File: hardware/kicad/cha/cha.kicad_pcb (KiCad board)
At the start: 4 copper layers, 173 x 134 mm, 115 parts, among them J1 AES_CHA, J2 CONF C, J3 CONF SM, J4 Câble PROG-CHA, U1 AMS1117-3.3, U10 74AHCT1G32, U11 74LVC1G07, U12 iCE40HX4K-TQ144, U13 AS4C32M16SB-6TIN, U14 iCE40HX4K-TQ144, U15 IS61WV10248EDBLL-10TLI, U2 AP2112K-1.2, U3 74LVC16244A, U4 74LVC16244A, U5 74LVC16244A, U6 74LVC16244A, U7 74AHCT16244, U8 74AHCT16244, U9 74AHCT244, X1 25 MHz 3,3 V, X2 25 MHz 3,3 V

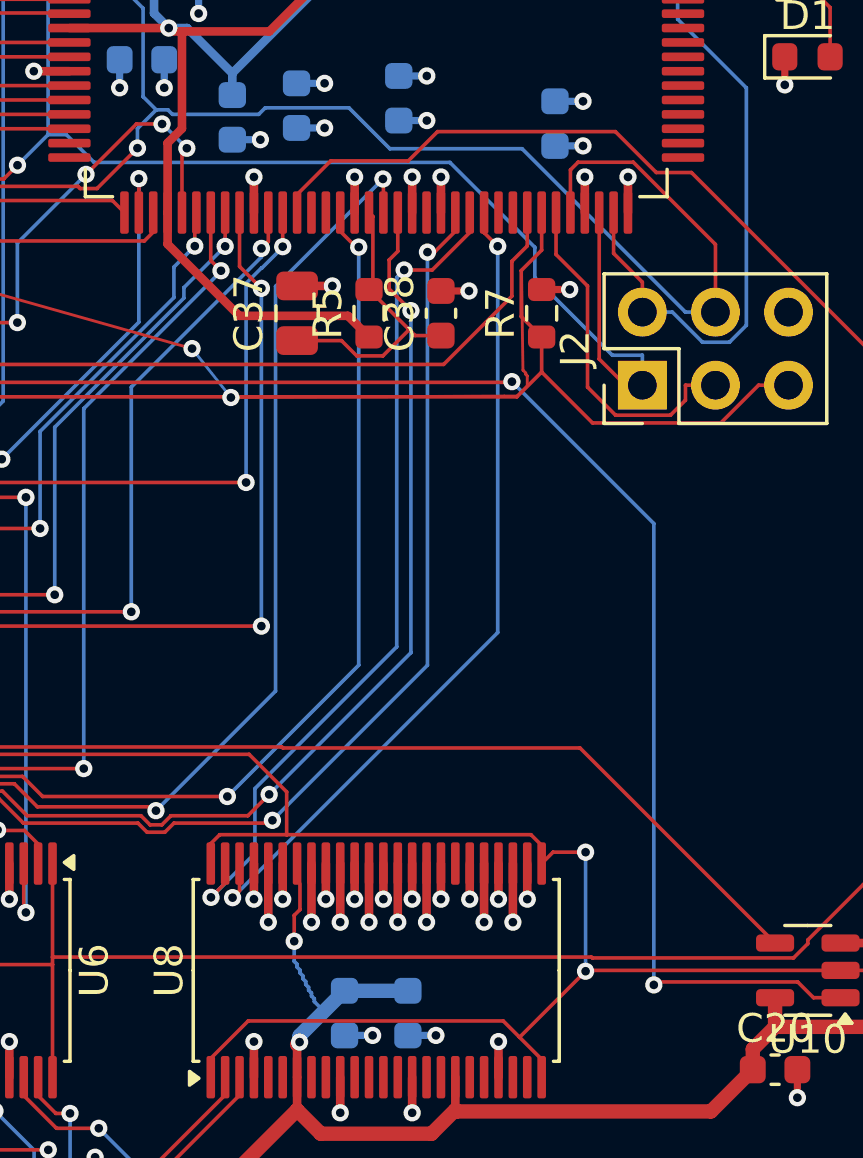
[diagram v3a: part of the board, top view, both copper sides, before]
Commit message: Carte CHA entièrement routée (dernière liaison : +5V de U8)
Sous U8 (2 canaux utilisés sur 16), les vias de masse des entrées
inutilisées enfermaient la broche 31 (+5V). La broche 32 (masse) est
reliée à sa voisine 33 au lieu d'avoir son propre via, ce qui libère
le passage ; +5V routé par le routeur de finition. DRC des deux cartes :
aucune liaison manquante, aucune violation de cuivre.

Co-Authored-By: Claude Opus 5.5 <noreply@anthropic.com>
Claude-Session: https://claude.ai/code/session_01WKfXP1YJ8otGxZ5dsY6Agh
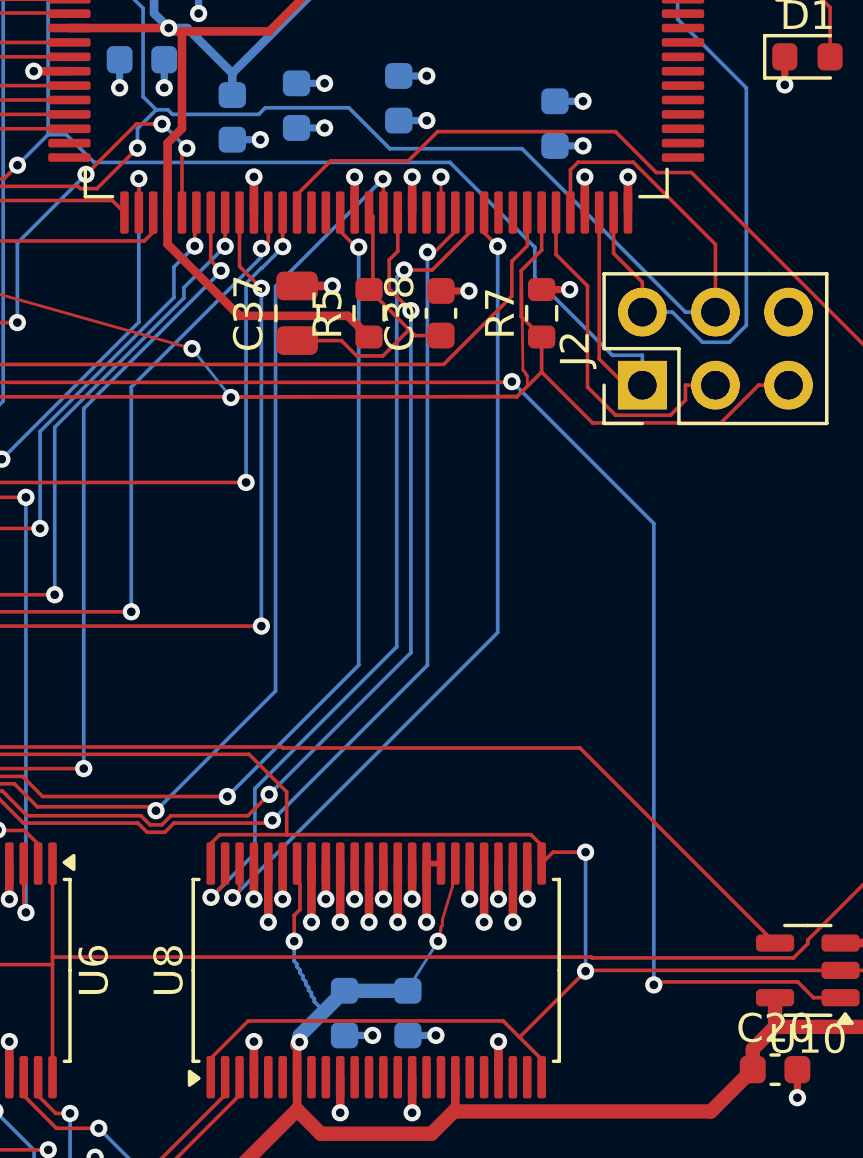
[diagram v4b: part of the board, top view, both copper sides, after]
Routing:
- net +5V: track 249.0 -> 252.9 mm, vias 10 -> 11
- net GND: track 280.6 -> 278.8 mm, vias 196 -> 195
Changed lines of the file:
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@@
   (segment (start 147.3861 152.3) (end 154.6675 145.0186) (width 0.5) (layer "F.Cu") (net 3))
   (segment (start 114.4486 129.1682) (end 98.7693 129.1682) (width 0.5) (layer "F.Cu") (net 3))
+  (segment (start 194.3 133.2375) (end 194.65 132.0875) (width 0.1) (layer "F.Cu") (net 3))
   (segment (start 147.3685 158.4735) (end 144.8815 158.4735) (width 0.5) (layer "F.Cu") (net 3))
   (segment (start 115.0342 129.7538) (end 115.9427 128.8453) (width 0.5) (layer "F.Cu") (net 3))
@@
   (segment (start 144.3732 152.3) (end 137.8767 145.8035) (width 0.5) (layer "F.Cu") (net 3))
   (segment (start 121.25 137.4558) (end 121.25 137.2725) (width 0.5) (layer "F.Cu") (net 3))
+  (segment (start 194.3 133.4375) (end 194.3 133.2375) (width 0.1) (layer "F.Cu") (net 3))
   (segment (start 115.9427 128.8453) (end 119.9477 128.8453) (width 0.5) (layer "F.Cu") (net 3))
   (segment (start 126.75 130.1476) (end 126.75 131.2875) (width 0.3004) (layer "F.Cu") (net 3))
+  (segment (start 194.15 133.9875) (end 194.25 133.5875) (width 0.1) (layer "F.Cu") (net 3))
   (segment (start 121.25 137.5726) (end 121.25 138.7125) (width 0.3004) (layer "F.Cu") (net 3))
   (segment (start 190.0739 140.6763) (end 189.25 139.8524) (width 0.5) (layer "F.Cu") (net 3))
+  (segment (start 194.65 132.0875) (end 194.65 131.9875) (width 0.1) (layer "F.Cu") (net 3))
   (segment (start 126.6515 130.0491) (end 125.9519 130.0491) (width 0.5) (layer "F.Cu") (net 3))
   (segment (start 115.0342 129.7538) (end 114.4486 129.1682) (width 0.5) (layer "F.Cu") (net 3))
@@
   (segment (start 126.75 139.8524) (end 126.75 138.7125) (width 0.3004) (layer "F.Cu") (net 3))
   (segment (start 147.795 158.9) (end 147.3685 158.4735) (width 0.5) (layer "F.Cu") (net 3))
+  (segment (start 194.25 133.5875) (end 194.25 133.4875) (width 0.1) (layer "F.Cu") (net 3))
   (segment (start 95.8133 132.1242) (end 95.8625 132.075) (width 0.4006) (layer "F.Cu") (net 3))
   (segment (start 189.25 137.5796) (end 189.25 138.7125) (width 0.3004) (layer "F.Cu") (net 3))
@@
   (segment (start 121.25 130.1476) (end 121.25 131.2875) (width 0.3004) (layer "F.Cu") (net 3))
   (segment (start 205.8625 136.9625) (end 205.0875 137.7375) (width 0.5) (layer "F.Cu") (net 3))
+  (segment (start 194.25 133.4875) (end 194.3 133.4375) (width 0.1) (layer "F.Cu") (net 3))
   (via (at 144.1433 160.3551) (size 0.6) (drill 0.3) (layers "F.Cu" "B.Cu") (net 3))
+  (via (at 194.15 133.9875) (size 0.6) (drill 0.3) (layers "F.Cu" "B.Cu") (net 3))
   (via (at 132.4705 145.8035) (size 0.6) (drill 0.3) (layers "F.Cu" "B.Cu") (net 3))
   (via (at 189.3373 137.4923) (size 0.6) (drill 0.3) (layers "F.Cu" "B.Cu") (net 3))
@@
   (segment (start 189.35 134.9875) (end 189.35 135.0875) (width 0.127) (layer "B.Cu") (net 3))
   (segment (start 193.1 135.71) (end 190.9 135.71) (width 0.5) (layer "B.Cu") (net 3))
+  (segment (start 193.2 135.4875) (end 194.15 133.9875) (width 0.1) (layer "B.Cu") (net 3))
   (segment (start 144.1433 160.3551) (end 144.3732 160.1252) (width 0.5) (layer "B.Cu") (net 3))
   (segment (start 189.75 135.8875) (end 189.85 135.9875) (width 0.127) (layer "B.Cu") (net 3))
@@
   (segment (start 101.338 91.25) (end 101.3375 91.25) (width 0.127) (layer "F.Cu") (net 162))
   (segment locked (start 162.25 131.2875) (end 162.25 132.525) (width 0.3) (layer "F.Cu") (net 162))
-  (segment (start 194.25 108.662) (end 194.25 108.6625) (width 0.127) (layer "F.Cu") (net 162))
   (segment locked (start 188.25 131.2875) (end 188.25 133.324999) (width 0.3) (layer "F.Cu") (net 162))
   (segment locked (start 189.75 82.8875) (end 190.975 82.8875) (width 0.3) (layer "F.Cu") (net 162))
@@
   (segment locked (start 190.75 131.2875) (end 190.75 133.324999) (width 0.3) (layer "F.Cu") (net 162))
   (segment locked (start 197.25 131.2875) (end 197.25 132.525) (width 0.3) (layer "F.Cu") (net 162))
-  (segment (start 194.25 131.288) (end 194.25 131.2875) (width 0.127) (layer "F.Cu") (net 162))
   (segment (start 189.75 131.288) (end 189.75 131.2875) (width 0.127) (layer "F.Cu") (net 162))
   (segment locked (start 193.25 131.2875) (end 193.25 132.525) (width 0.3) (layer "F.Cu") (net 162))
@@
   (segment locked (start 114.25 108.6625) (end 114.25 107.425) (width 0.3) (layer "F.Cu") (net 162))
   (segment locked (start 172.75 138.7125) (end 172.75 137.475) (width 0.3) (layer "F.Cu") (net 162))
-  (segment locked (start 194.25 131.2875) (end 194.25 132.525) (width 0.3) (layer "F.Cu") (net 162))
   (segment (start 175.25 138.712) (end 175.25 138.7125) (width 0.127) (layer "F.Cu") (net 162))
   (segment (start 171.25 138.712) (end 171.25 138.7125) (width 0.127) (layer "F.Cu") (net 162))
@@
   (segment locked (start 114.75 83.0625) (end 115.725 83.0625) (width 0.25) (layer "F.Cu") (net 162))
   (segment locked (start 173.75 138.7125) (end 173.75 137.475) (width 0.3) (layer "F.Cu") (net 162))
-  (segment locked (start 194.25 108.6625) (end 194.25 107.425) (width 0.3) (layer "F.Cu") (net 162))
   (segment locked (start 101.3375 91.25) (end 102.575 91.25) (width 0.3) (layer "F.Cu") (net 162))
+  (segment locked (start 194.25 131.2875) (end 193.75 131.2875) (width 0.2) (layer "F.Cu") (net 162))
   (segment (start 208.538 97.85) (end 208.5375 97.85) (width 0.127) (layer "F.Cu") (net 162))
   (segment locked (start 191.25 131.2875) (end 191.25 132.525) (width 0.3) (layer "F.Cu") (net 162))
@@
   (segment locked (start 111.25 108.6625) (end 111.25 107.425) (width 0.3) (layer "F.Cu") (net 162))
   (segment locked (start 159.25 131.2875) (end 159.25 130.049999) (width 0.3) (layer "F.Cu") (net 162))
+  (segment (start 194.25 107.725) (end 194.25 107.925) (width 0.1) (layer "F.Cu") (net 162))
   (segment locked (start 187.75 131.2875) (end 187.75 132.525) (width 0.3) (layer "F.Cu") (net 162))
   (segment locked (start 145.505 159.4) (end 145.505 160.375) (width 0.25) (layer "F.Cu") (net 162))
@@
   (via locked (at 199.447358 98.505665) (size 0.6) (drill 0.3) (layers "F.Cu" "B.Cu") (net 162))
   (via locked (at 170.75 137.475) (size 0.6) (drill 0.3) (layers "F.Cu" "B.Cu") (net 162))
-  (via locked (at 194.25 132.525) (size 0.6) (drill 0.3) (layers "F.Cu" "B.Cu") (net 162))
   (via locked (at 143.825 147.4) (size 0.6) (drill 0.3) (layers "F.Cu" "B.Cu") (net 162))
   (via locked (at 178.25 137.475) (size 0.6) (drill 0.3) (layers "F.Cu" "B.Cu") (net 162))

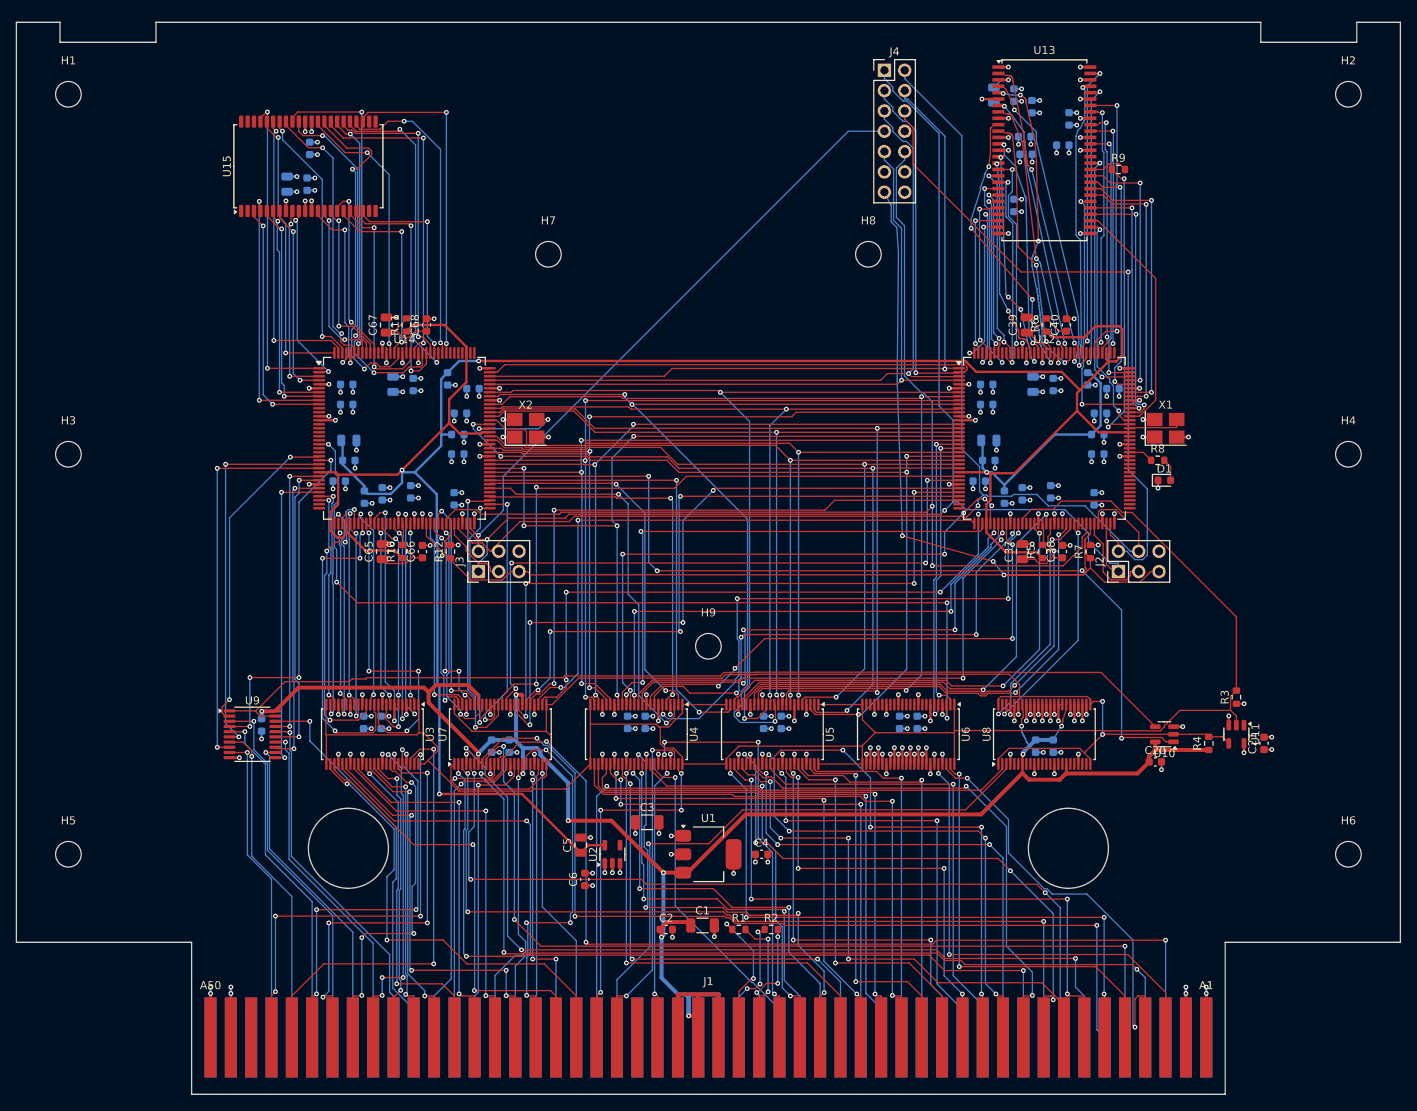
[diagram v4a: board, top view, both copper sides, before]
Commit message: Régulateur 3,3 V à découpage, horloge SDRAM adaptée côté FPGA, U8 en 74AHCT125
- AP63203 (TSOT-23-6, sortie fixe 3,3 V, ~90 %) à la place de
  l'AMS1117 : ~0,15 W de pertes au lieu de ~0,75 W et moins de courant
  tiré sur le 5 V de la console ; L 4,7 µH, Cin 10 µF, Cout 2 x 22 µF.
- Résistance série de 33 ohms de l'horloge SDRAM déclarée avec le FPGA :
  placée à 2,7 mm de sa broche (au lieu de ~30 mm, côté SDRAM).
- CHA : U8 (16244 pour 2 canaux) remplacé par un 74AHCT125.
Cartes replacées, contrôle Freerouting sans violation ; routage des
deux cartes et vérification de timing en cours.

Co-Authored-By: Claude Opus 5.5 <noreply@anthropic.com>
Claude-Session: https://claude.ai/code/session_01WKfXP1YJ8otGxZ5dsY6Agh
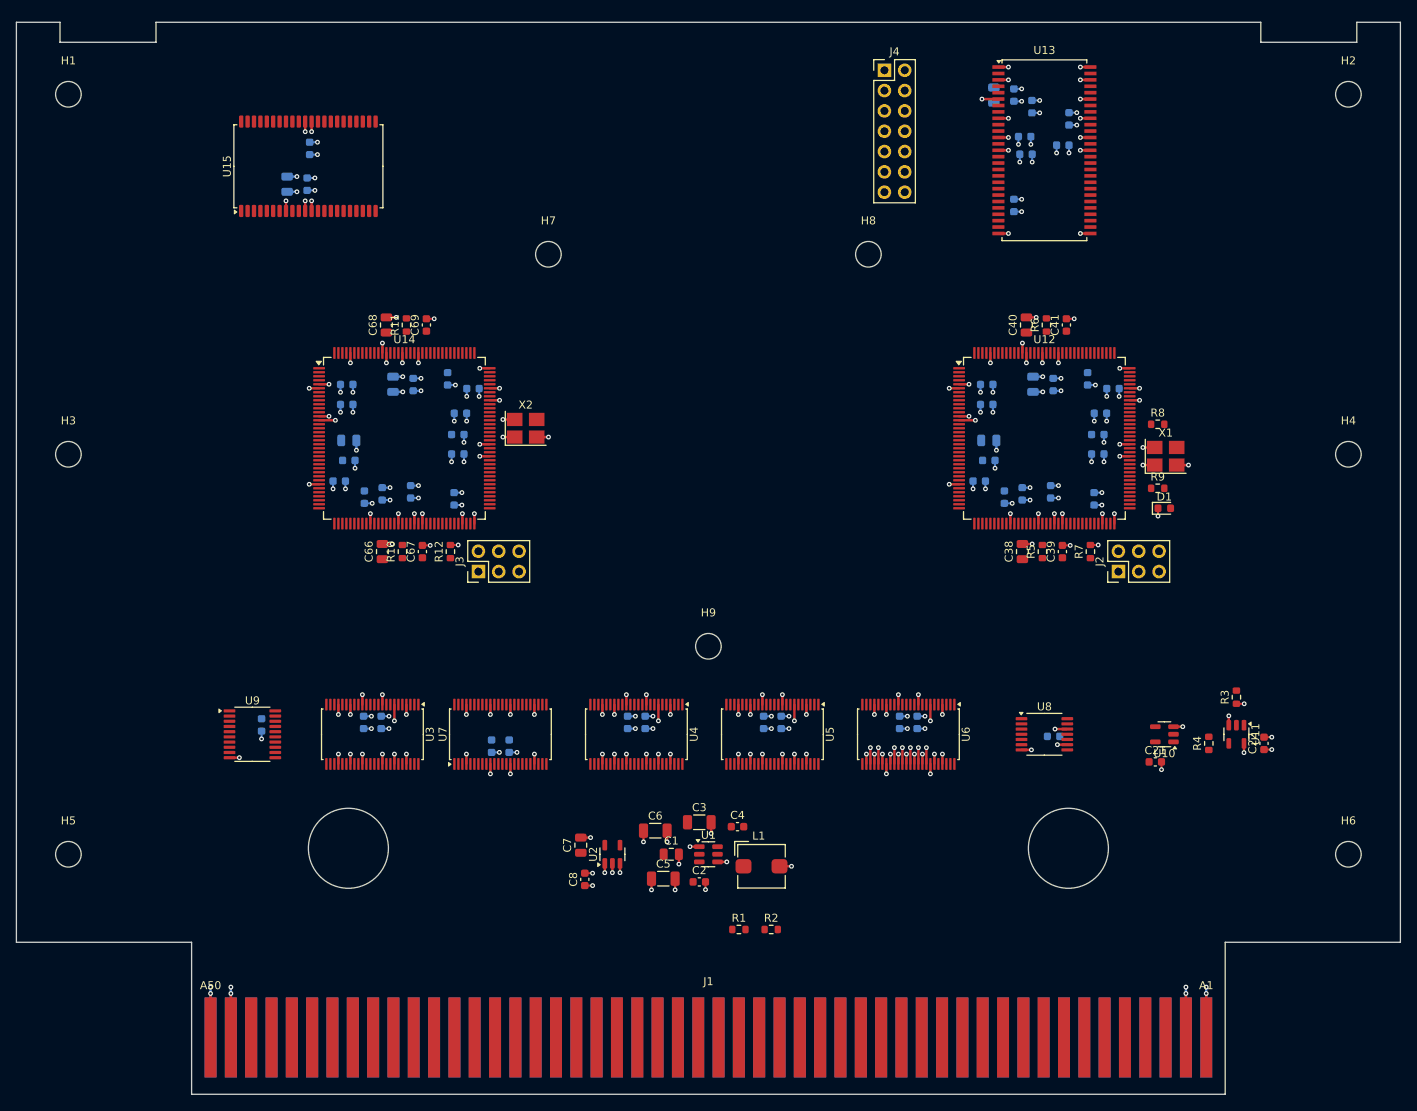
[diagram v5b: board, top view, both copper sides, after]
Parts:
- added C73: 10u, Capacitor_SMD:C_0805_2012Metric, B.Cu at (97.3, 66.2)
- added L1: 4,7 µH 3 A, Inductor_SMD:L_Bourns_SRP5030T, F.Cu at (156.6, 151.5)
- C1: value 22u -> 10u; footprint Capacitor_SMD:C_1206_3216Metric -> Capacitor_SMD:C_0805_2012Metric
- C20, C37, C65: moved to B.Cu
- C22, C41, C69: moved to F.Cu
- C26, C36, C39, C49, C54, C64, C67, C72: value 10u -> 100n; footprint Capacitor_SMD:C_0805_2012Metric -> Capacitor_SMD:C_0603_1608Metric
- C27, C38, C40, C50, C55, C66, C68: value 100n -> 10u; footprint Capacitor_SMD:C_0603_1608Metric -> Capacitor_SMD:C_0805_2012Metric
- C5: value 10u -> 22u; footprint Capacitor_SMD:C_0805_2012Metric -> Capacitor_SMD:C_1206_3216Metric
- C6: value 1u -> 22u; footprint Capacitor_SMD:C_0603_1608Metric -> Capacitor_SMD:C_1206_3216Metric
- C7: value 100n -> 10u; footprint Capacitor_SMD:C_0603_1608Metric -> Capacitor_SMD:C_0805_2012Metric; moved to F.Cu
- C8: value 100n -> 1u; moved to F.Cu
- R8: value 470 -> 33
- R9: value 33 -> 470
- U1: value AMS1117-3.3 -> AP63203WU; footprint Package_TO_SOT_SMD:SOT-223-3_TabPin2 -> Package_TO_SOT_SMD:TSOT-23-6
- U8: value 74AHCT16244 -> 74AHCT125; footprint Package_SO:TSSOP-48_6.1x12.5mm_P0.5mm -> Package_SO:TSSOP-14_4.4x5mm_P0.65mm
- moved C20 111.8 mm to (94.1, 133.8), turned to -90 degrees
- moved C19 99.0 mm to (193.1, 135.3), turned to 0 degrees
- moved C50 92.7 mm to (185.7, 55.1), turned to -90 degrees
- moved C17 68.0 mm to (122.9, 136.5)
- moved C18 68.0 mm to (125.1, 136.5)
- moved C15 53.3 mm to (176.1, 133.5)
- moved C22 49.3 mm to (219.4, 136.1), turned to 90 degrees
- moved C16 48.9 mm to (173.9, 133.5)
- moved R9 40.2 mm to (206.2, 104.2)
- moved C42 36.3 mm to (184.8, 91.3), turned to 0 degrees
- moved C8 33.9 mm to (134.6, 153.1), turned to 90 degrees
- moved C10 33.0 mm to (106.9, 133.5)
- moved C9 33.0 mm to (109.1, 133.5)
- moved C7 29.3 mm to (134.1, 148.9), turned to 90 degrees
- moved C39 28.7 mm to (194.2, 112.2)
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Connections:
- C15 pad 1: +5V -> +3V3
- C16 pad 1: +5V -> +3V3
- C21 pad 1: +3V3 -> +5V
- C22 pad 1: +1V2 -> +3V3
- C27 pad 1: +3V3 -> +1V2
- C3 pad 1: +3V3 -> +5V
- C37 pad 1: C_VCCPLL0 -> +3V3
- C39 pad 1: C_VCCPLL1 -> C_VCCPLL0
- C4 pad 1: +3V3 -> BST33
- C4 pad 2: GND -> SW33
- C41 pad 1: +3V3 -> C_VCCPLL1
- C5 pad 1: +1V2 -> +3V3
- C50 pad 1: +1V2 -> +3V3
- C55 pad 1: +3V3 -> +1V2
- C65 pad 1: SM_VCCPLL0 -> +3V3
- C67 pad 1: SM_VCCPLL1 -> SM_VCCPLL0
- C69 pad 1: +3V3 -> SM_VCCPLL1
- C7 pad 1: +3V3 -> +1V2
- R8 pad 1: C_LED -> C_SD_CLK
- R8 pad 2: C_LED_K -> C_SD_CLK_R
- R9 pad 1: C_SD_CLK -> C_LED
- R9 pad 2: C_SD_CLK_R -> C_LED_K
- U1 pad 1: GND -> +3V3
- U1 pad 2: +3V3 -> +5V
- U12 pad 10: P2 -> P12
- U12 pad 12: P12 -> P10
- U12 pad 8: P1 -> P2
- U12 pad 81: (no net) -> C_LED
- U12 pad 87: C_LED -> (no net)
- U12 pad 9: P10 -> P1
- U14 pad 101: P2 -> P1
- U14 pad 85: P10 -> P12
- U14 pad 88: P12 -> P9
- U14 pad 90: P9 -> P10
- U14 pad 99: P1 -> P2
- U8 pad 10: GND -> +5V
- U8 pad 12: (no net) -> GND
- U8 pad 13: (no net) -> +5V
- U8 pad 14: (no net) -> +5V
- U8 pad 2: AES_DOTB -> DOTB
- U8 pad 3: AES_DOTA -> AES_DOTB
- U8 pad 4: GND -> OE5_N
- U8 pad 5: (no net) -> DOTA
- U8 pad 6: (no net) -> AES_DOTA
- U8 pad 7: +5V -> GND
- U8 pad 9: (no net) -> GND
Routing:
- net +1V2: track 338.8 -> 0.00 mm, vias 4 -> 0
- net +5V: track 252.9 -> 0.00 mm, vias 11 -> 0
- net XLAT_EN_N: track 230.4 -> 0.00 mm
- net CRESET_N: track 174.1 -> 0.00 mm, vias 3 -> 0
- net CHA_IO0: track 161.7 -> 0.00 mm, vias 1 -> 0
- net CHA_SCK: track 158.7 -> 0.00 mm, vias 2 -> 0
- net OE5_N: track 153.2 -> 0.00 mm, vias 2 -> 0
- net CDONE: track 139.5 -> 0.00 mm, vias 2 -> 0
- net SDD_OE5_N: track 123.3 -> 0.00 mm
- net AES_FIXD0: track 119.6 -> 0.00 mm, vias 3 -> 0
- net P1: track 117.1 -> 0.00 mm, vias 2 -> 0
- net AES_FIXD1: track 116.1 -> 0.00 mm, vias 3 -> 0
- net SDD_OE_N: track 115.0 -> 0.00 mm, vias 4 -> 0
- net AES_FIXD2: track 114.8 -> 0.00 mm, vias 3 -> 0
- net AES_FIXD3: track 113.1 -> 0.00 mm, vias 3 -> 0
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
